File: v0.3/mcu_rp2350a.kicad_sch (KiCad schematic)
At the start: 33 parts, among them SW4 RUN, SW5 BOOTSEL, U1 RP2350A-QFN60, Y1 ABM8-272-T3, Y2 SIT1533AI-H4-DCC-32.768E

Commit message: v0.3: lots of routing done
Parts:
- removed NT4: NetTie_2, symbol Device:NetTie_2
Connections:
- net MCU_3V3 is gone; now on net +3.3V: C27.1, C28.1, C29.1, C30.1, C31.1, C32.1, C33.1, C35.1, R33.1, U1.1 (IOVDD), U1.11 (IOVDD), U1.20 (IOVDD), U1.30 (IOVDD), U1.38 (IOVDD), U1.44 (ADC_AVDD), U1.45 (IOVDD), U1.49 (VREG_VIN), U1.53 (USB_OTP_VDD), U1.54 (QSPI_IOVDD), Y2.4 (VDD)
- net PWR_AUX.~{BAT_CE}: now also U1.40 (GPIO26_ADC0); no longer U1.41 (GPIO27_ADC1)
- net PWR_AUX.~{BAT_INT}: now also U1.41 (GPIO27_ADC1); no longer U1.40 (GPIO26_ADC0)
- net SCREEN_AUX.~{CSB}: now also U1.9 (GPIO6); no longer U1.10 (GPIO7)
- net SCREEN_AUX.~{RST}: now also U1.10 (GPIO7); no longer U1.9 (GPIO6)
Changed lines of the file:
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@@
 	(wire
 		(pts
-			(xy 99.06 22.86) (xy 102.87 22.86)
+			(xy 99.06 22.86) (xy 127 22.86)
 		)
 		(stroke
@@
 	(wire
 		(pts
-			(xy 107.95 22.86) (xy 127 22.86)
-		)
-		(stroke
-			(width 0)
-			(type default)
-		)
-	)
-	(wire
-		(pts
 			(xy 74.93 153.67) (xy 74.93 158.75)
 		)
@@
 			(width 0)
 			(type default)
-		)
-	)
-	(label "PWR_AUX.~{BAT_INT}"
-		(at 219.71 114.3 0)
-		(effects
-			(font
-				(size 1.27 1.27)
-			)
-			(justify left bottom)
 		)
 	)
@@
 		)
 	)
+	(label "PWR_AUX.~{BAT_CE}"
+		(at 219.71 114.3 0)
+		(effects
+			(font
+				(size 1.27 1.27)
+			)
+			(justify left bottom)
+		)
+	)
+	(label "SCREEN_AUX.~{RST}"
+		(at 213.36 63.5 0)
+		(effects
+			(font
+				(size 1.27 1.27)
+			)
+			(justify left bottom)
+		)
+	)
 	(label "MCU_3V3"
 		(at 91.44 179.07 0)
@@
 		)
 	)
-	(label "SCREEN_AUX.~{RST}"
-		(at 213.36 60.96 0)
-		(effects
-			(font
-				(size 1.27 1.27)
-			)
-			(justify left bottom)
-		)
-	)
 	(label "USB.D+"
 		(at 232.41 33.02 0)
@@
 		)
 	)
-	(label "SCREEN_AUX.~{CSB}"
-		(at 213.36 63.5 0)
-		(effects
-			(font
-				(size 1.27 1.27)
-			)
-			(justify left bottom)
-		)
-	)
 	(label "VREG_PGND"
 		(at 39.37 58.42 90)
@@
 		)
 	)
+	(label "PWR_AUX.~{BAT_INT}"
+		(at 219.71 116.84 0)
+		(effects
+			(font
+				(size 1.27 1.27)
+			)
+			(justify left bottom)
+		)
+	)
 	(label "MCU_3V3"
 		(at 163.83 20.32 0)
@@
 		)
 	)
+	(label "SCREEN_AUX.~{CSB}"
+		(at 213.36 60.96 0)
+		(effects
+			(font
+				(size 1.27 1.27)
+			)
+			(justify left bottom)
+		)
+	)
 	(label "I2C.SCL"
 		(at 219.71 121.92 0)
@@
 	(label "SCREEN_AUX.PWR_EN"
 		(at 213.36 58.42 0)
-		(effects
-			(font
-				(size 1.27 1.27)
-			)
-			(justify left bottom)
-		)
-	)
-	(label "PWR_AUX.~{BAT_CE}"
-		(at 219.71 116.84 0)
 		(effects
 			(font
@@
 		)
 	)
-	(hierarchical_label "PWR_AUX{~{BAT_CE}, ~{BAT_INT}}"
-		(shape bidirectional)
-		(at 241.3 114.3 0)
-		(effects
-			(font
-				(size 1.27 1.27)
-			)
-			(justify left)
-		)
-	)
 	(hierarchical_label "SOUND_PWM"
 		(shape output)
@@
 		)
 	)
-	(hierarchical_label "PWR_AUX{~{BAT_CE}, ~{BAT_INT}}"
+	(hierarchical_label "PWR_AUX{~{BAT_CE}, ~{BAT_INT}, ~{PG}}"
 		(shape bidirectional)
 		(at 241.3 119.38 0)
@@
 		)
 	)
+	(hierarchical_label "PWR_AUX{~{BAT_CE}, ~{BAT_INT}, ~{PG}}"
+		(shape bidirectional)
+		(at 241.3 114.3 0)
+		(effects
+			(font
+				(size 1.27 1.27)
+			)
+			(justify left)
+		)
+	)
 	(hierarchical_label "~{ACCEL_CSB}"
 		(shape output)
@@
 		)
 	)
-	(hierarchical_label "PWR_AUX{~{BAT_CE}, ~{BAT_INT}}"
+	(hierarchical_label "PWR_AUX{~{BAT_CE}, ~{BAT_INT}, ~{PG}}"
 		(shape bidirectional)
 		(at 241.3 116.84 0)
@@
 					(unit 1)
 				)
-			)
-		)
-	)
-	(symbol
-		(lib_id "Device:NetTie_2")
-		(at 105.41 22.86 0)
-		(unit 1)
-		(exclude_from_sim no)
-		(in_bom no)
-		(on_board yes)
-		(dnp no)
-		(fields_autoplaced yes)
-		(property "Reference" "NT4"
-			(at 105.41 17.78 0)
-			(effects
-				(font
-					(size 1.27 1.27)
-				)
-			)
-		)
-		(property "Value" "NetTie_2"
-			(at 105.41 20.32 0)
-			(effects
-				(font
-					(size 1.27 1.27)
-				)
-			)
-		)
-		(property "Footprint" ""
-			(at 105.41 22.86 0)
-			(effects
-				(font
-					(size 1.27 1.27)
-				)
-				(hide yes)
-			)
-		)
-		(property "Datasheet" "~"
-			(at 105.41 22.86 0)
-			(effects
-				(font
-					(size 1.27 1.27)
-				)
-				(hide yes)
-			)
-		)
-		(property "Description" "Net tie, 2 pins"
-			(at 105.41 22.86 0)
-			(effects
-				(font
-					(size 1.27 1.27)
-				)
-				(hide yes)
-			)
-		)
-		(pin "1"
-		)
-		(pin "2"
-		)
-		(instances
-			(project ""
-				(path "/5cbb45d4-7f83-48dd-a53b-5c75c7d1d827/43898cce-4488-4636-8fe4-d95251b1544a"
-					(reference "NT4")
-					(unit 1)
-				)

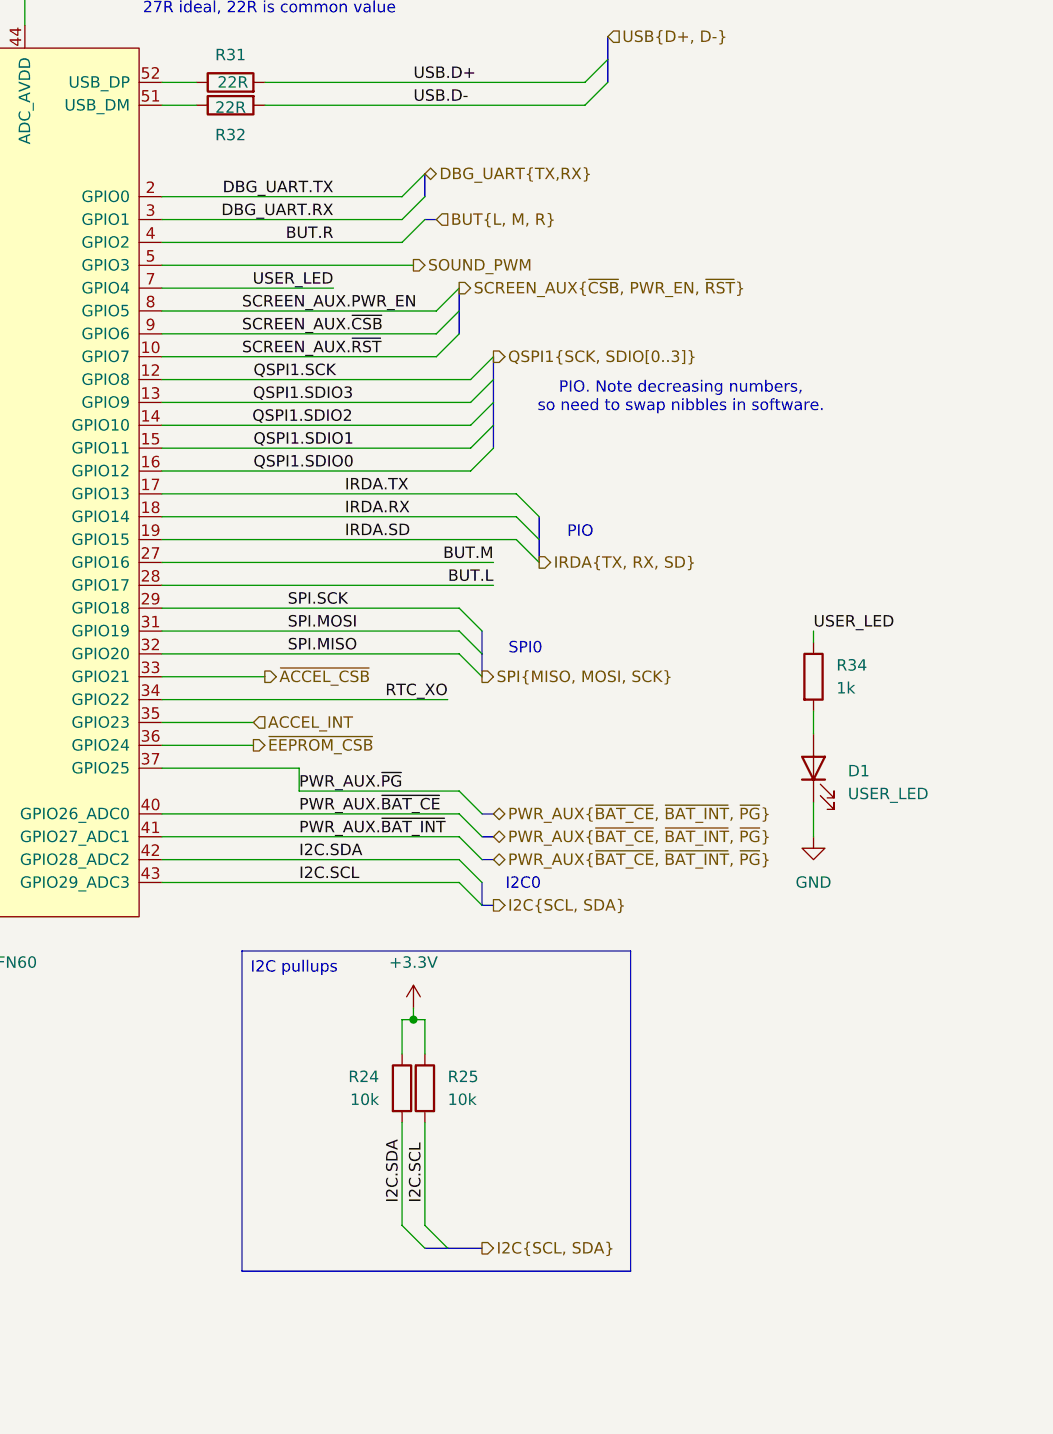
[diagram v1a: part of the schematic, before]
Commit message: v0.3: DRC checks mostly pass, onto final tweaks
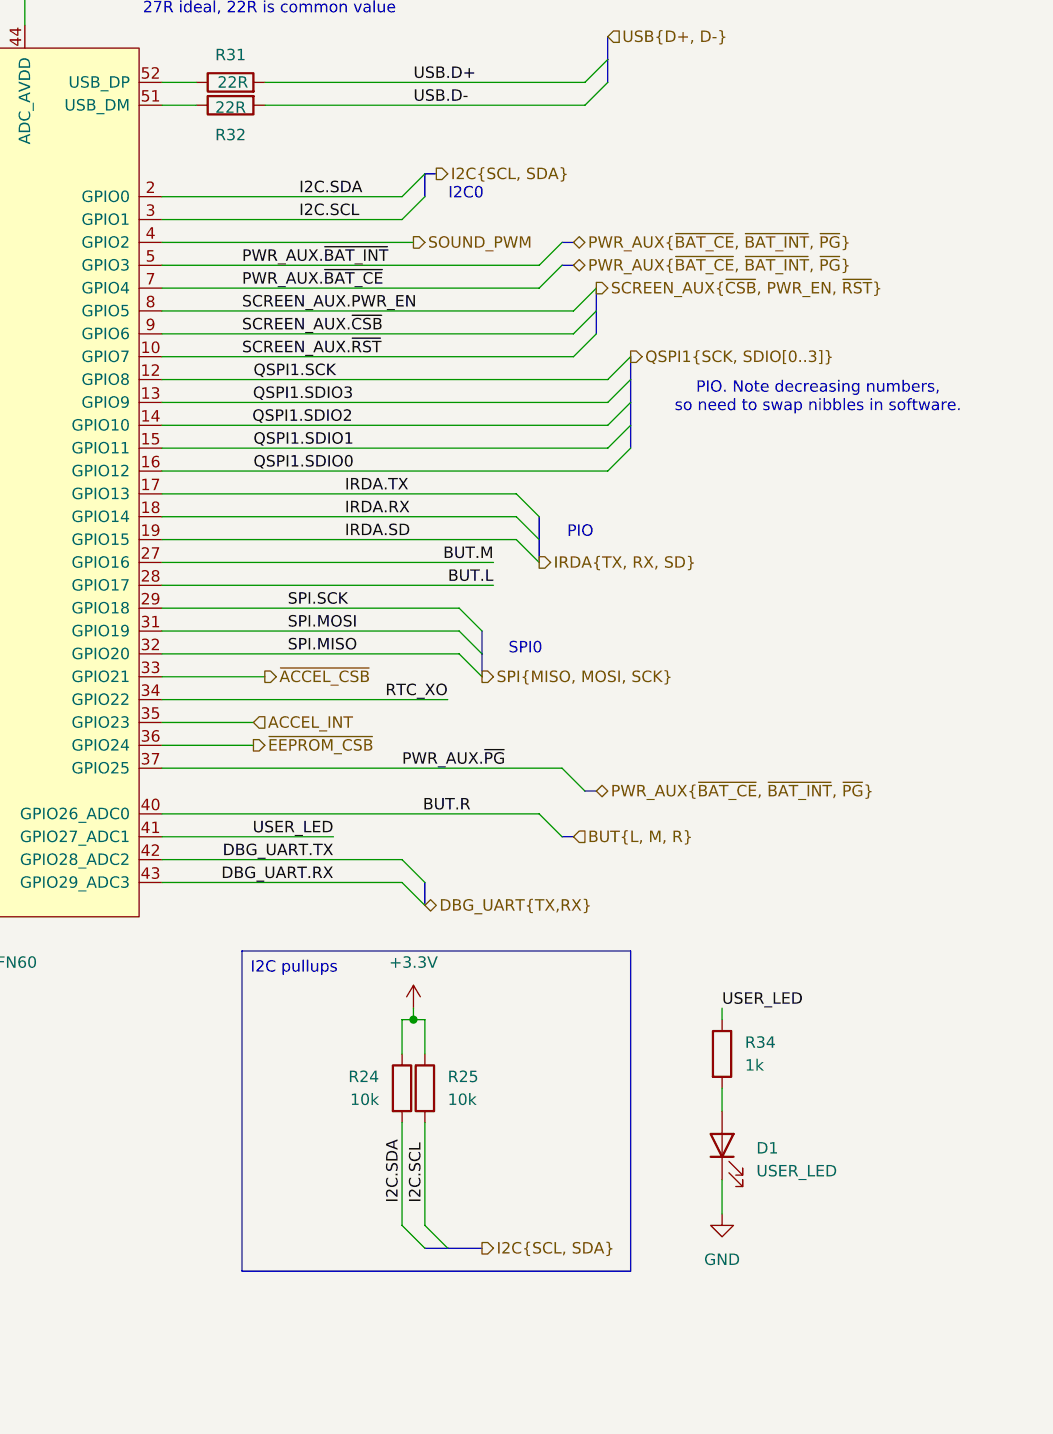
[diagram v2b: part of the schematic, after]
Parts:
- TP2: footprint TestPoint:TestPoint_Pad_2.5x2.5mm -> TestPoint:TestPoint_Pad_1.0x1.0mm
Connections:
- net BUT.R: now also U1.40 (GPIO26_ADC0); no longer U1.4 (GPIO2)
- net DBG_UART.RX: now also U1.43 (GPIO29_ADC3); no longer U1.3 (GPIO1)
- net DBG_UART.TX: now also U1.42 (GPIO28_ADC2); no longer U1.2 (GPIO0)
- net I2C.SCL: now also U1.3 (GPIO1); no longer U1.43 (GPIO29_ADC3)
- net I2C.SDA: now also U1.2 (GPIO0); no longer U1.42 (GPIO28_ADC2)
- net PWR_AUX.~{BAT_CE}: now also U1.7 (GPIO4); no longer U1.40 (GPIO26_ADC0)
- net PWR_AUX.~{BAT_INT}: now also U1.5 (GPIO3); no longer U1.41 (GPIO27_ADC1)
- net SOUND_PWM: now also U1.4 (GPIO2); no longer U1.5 (GPIO3)
- net USER_LED: now also U1.41 (GPIO27_ADC1); no longer U1.7 (GPIO4)
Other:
- moved on the sheet: D1, R34
